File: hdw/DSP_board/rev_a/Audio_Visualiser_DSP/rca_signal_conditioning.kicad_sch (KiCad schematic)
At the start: 17 parts, among them J4 Left, J5 Right

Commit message: Annotated schematic
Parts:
- renumbered C62 to C1301, C63 to C1302, D14 to D1301, D15 to D1302, D16 to D1303, D17 to D1304, J4 to J1301, J5 to J1302, NT1 to NT1301, R61 to R1301, R62 to R1302, R63 to R1303, R64 to R1304, R65 to R1305, R66 to R1306, V1 to V1301, V6 to V1302
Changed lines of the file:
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@@
 		(dnp no)
 		(fields_autoplaced yes)
-		(property "Reference" "#PWR0221"
+		(property "Reference" "#PWR01306"
 			(at 149.86 55.88 0)
 			(hide yes)
@@
 			(project "Audio_Visualiser_DSP"
 				(path "/97a4dfb8-0e16-46f1-9709-8d2007dd0cd3/363750b9-a522-47db-9c7c-ad0a11bbbf3f"
-					(reference "#PWR0221")
+					(reference "#PWR01306")
 					(unit 1)
 				)
@@
 		(in_pos_files yes)
 		(dnp no)
-		(property "Reference" "#PWR0217"
+		(property "Reference" "#PWR01301"
 			(at 86.36 88.9 0)
 			(hide yes)
@@
 			(project "Audio_Visualiser_DSP"
 				(path "/97a4dfb8-0e16-46f1-9709-8d2007dd0cd3/363750b9-a522-47db-9c7c-ad0a11bbbf3f"
-					(reference "#PWR0217")
+					(reference "#PWR01301")
 					(unit 1)
 				)
@@
 		(in_pos_files yes)
 		(dnp no)
-		(property "Reference" "#PWR0314"
+		(property "Reference" "#PWR01302"
 			(at 86.36 152.4 0)
 			(hide yes)
@@
 			(project "Audio_Visualiser_DSP"
 				(path "/97a4dfb8-0e16-46f1-9709-8d2007dd0cd3/363750b9-a522-47db-9c7c-ad0a11bbbf3f"
-					(reference "#PWR0314")
+					(reference "#PWR01302")
 					(unit 1)
 				)
@@
 		(in_pos_files yes)
 		(dnp no)
-		(property "Reference" "V6"
+		(property "Reference" "V1302"
 			(at 88.9 138.43 0)
 			(show_name no)
@@
 			(project "Audio_Visualiser_DSP"
 				(path "/97a4dfb8-0e16-46f1-9709-8d2007dd0cd3/363750b9-a522-47db-9c7c-ad0a11bbbf3f"
-					(reference "V6")
+					(reference "V1302")
 					(unit 1)
 				)
@@
 		(dnp no)
 		(fields_autoplaced yes)
-		(property "Reference" "#PWR0220"
+		(property "Reference" "#PWR01305"
 			(at 133.35 152.4 0)
 			(hide yes)
@@
 			(project "Audio_Visualiser_DSP"
 				(path "/97a4dfb8-0e16-46f1-9709-8d2007dd0cd3/363750b9-a522-47db-9c7c-ad0a11bbbf3f"
-					(reference "#PWR0220")
+					(reference "#PWR01305")
 					(unit 1)
 				)
@@
 		(dnp no)
 		(fields_autoplaced yes)
-		(property "Reference" "C62"
+		(property "Reference" "C1301"
 			(at 124.46 46.99 90)
 			(show_name no)
@@
 			(project "Audio_Visualiser_DSP"
 				(path "/97a4dfb8-0e16-46f1-9709-8d2007dd0cd3/363750b9-a522-47db-9c7c-ad0a11bbbf3f"
-					(reference "C62")
+					(reference "C1301")
 					(unit 1)
 				)
@@
 		(dnp no)
 		(fields_autoplaced yes)
-		(property "Reference" "C63"
+		(property "Reference" "C1302"
 			(at 124.46 110.49 90)
 			(show_name no)
@@
 			(project "Audio_Visualiser_DSP"
 				(path "/97a4dfb8-0e16-46f1-9709-8d2007dd0cd3/363750b9-a522-47db-9c7c-ad0a11bbbf3f"
-					(reference "C63")
+					(reference "C1302")
 					(unit 1)
 				)
@@
 		(in_pos_files yes)
 		(dnp no)
-		(property "Reference" "#PWR0218"
+		(property "Reference" "#PWR01303"
 			(at 115.57 78.74 0)
 			(hide yes)
@@
 			(project "Audio_Visualiser_DSP"
 				(path "/97a4dfb8-0e16-46f1-9709-8d2007dd0cd3/363750b9-a522-47db-9c7c-ad0a11bbbf3f"
-					(reference "#PWR0218")
+					(reference "#PWR01303")
 					(unit 1)
 				)
@@
 		(dnp no)
 		(fields_autoplaced yes)
-		(property "Reference" "#PWR0222"
+		(property "Reference" "#PWR01307"
 			(at 149.86 119.38 0)
 			(hide yes)
@@
 			(project "Audio_Visualiser_DSP"
 				(path "/97a4dfb8-0e16-46f1-9709-8d2007dd0cd3/363750b9-a522-47db-9c7c-ad0a11bbbf3f"
-					(reference "#PWR0222")
+					(reference "#PWR01307")
 					(unit 1)
 				)
@@
 		(dnp no)
 		(fields_autoplaced yes)
-		(property "Reference" "J4"
+		(property "Reference" "J1301"
 			(at 73.9774 55.88 0)
 			(show_name no)
@@
 			(project "Audio_Visualiser_DSP"
 				(path "/97a4dfb8-0e16-46f1-9709-8d2007dd0cd3/363750b9-a522-47db-9c7c-ad0a11bbbf3f"
-					(reference "J4")
+					(reference "J1301")
 					(unit 1)
 				)
@@
 		(in_pos_files yes)
 		(dnp no)
-		(property "Reference" "R64"
+		(property "Reference" "R1304"
 			(at 135.89 123.19 90)
 			(show_name no)
@@
 			(project "Audio_Visualiser_DSP"
 				(path "/97a4dfb8-0e16-46f1-9709-8d2007dd0cd3/363750b9-a522-47db-9c7c-ad0a11bbbf3f"
-					(reference "R64")
+					(reference "R1304")
 					(unit 1)
 				)
@@
 		(in_pos_files yes)
 		(dnp no)
-		(property "Reference" "#PWR0219"
+		(property "Reference" "#PWR01304"
 			(at 115.57 142.24 0)
 			(hide yes)
@@
 			(project "Audio_Visualiser_DSP"
 				(path "/97a4dfb8-0e16-46f1-9709-8d2007dd0cd3/363750b9-a522-47db-9c7c-ad0a11bbbf3f"
-					(reference "#PWR0219")
+					(reference "#PWR01304")
 					(unit 1)
 				)
@@
 		(in_pos_files yes)
 		(dnp no)
-		(property "Reference" "#PWR0226"
+		(property "Reference" "#PWR01311"
 			(at 177.8 139.7 0)
 			(hide yes)
@@
 			(project "Audio_Visualiser_DSP"
 				(path "/97a4dfb8-0e16-46f1-9709-8d2007dd0cd3/363750b9-a522-47db-9c7c-ad0a11bbbf3f"
-					(reference "#PWR0226")
+					(reference "#PWR01311")
 					(unit 1)
 				)
@@
 		(in_pos_files yes)
 		(dnp no)
-		(property "Reference" "R62"
+		(property "Reference" "R1302"
 			(at 99.06 123.19 90)
 			(show_name no)
@@
 			(project "Audio_Visualiser_DSP"
 				(path "/97a4dfb8-0e16-46f1-9709-8d2007dd0cd3/363750b9-a522-47db-9c7c-ad0a11bbbf3f"
-					(reference "R62")
+					(reference "R1302")
 					(unit 1)
 				)
@@
 		(dnp no)
 		(fields_autoplaced yes)
-		(property "Reference" "D14"
+		(property "Reference" "D1301"
 			(at 118.11 67.3099 90)
 			(show_name no)
@@
 			(project "Audio_Visualiser_DSP"
 				(path "/97a4dfb8-0e16-46f1-9709-8d2007dd0cd3/363750b9-a522-47db-9c7c-ad0a11bbbf3f"
-					(reference "D14")
+					(reference "D1301")
 					(unit 1)
 				)
@@
 		(dnp no)
 		(fields_autoplaced yes)
-		(property "Reference" "D15"
+		(property "Reference" "D1302"
 			(at 118.11 130.8099 90)
 			(show_name no)
@@
 			(project "Audio_Visualiser_DSP"
 				(path "/97a4dfb8-0e16-46f1-9709-8d2007dd0cd3/363750b9-a522-47db-9c7c-ad0a11bbbf3f"
-					(reference "D15")
+					(reference "D1302")
 					(unit 1)
 				)
@@
 		(in_pos_files yes)
 		(dnp no)
-		(property "Reference" "V1"
+		(property "Reference" "V1301"
 			(at 88.9 74.93 0)
 			(show_name no)
@@
 			(project "Audio_Visualiser_DSP"
 				(path "/97a4dfb8-0e16-46f1-9709-8d2007dd0cd3/363750b9-a522-47db-9c7c-ad0a11bbbf3f"
-					(reference "V1")
+					(reference "V1301")
 					(unit 1)
 				)
@@
 		(in_pos_files yes)
 		(dnp no)
-		(property "Reference" "D17"
+		(property "Reference" "D1304"
 			(at 180.34 121.92 90)
 			(show_name no)
@@
 			(project "Audio_Visualiser_DSP"
 				(path "/97a4dfb8-0e16-46f1-9709-8d2007dd0cd3/363750b9-a522-47db-9c7c-ad0a11bbbf3f"
-					(reference "D17")
+					(reference "D1304")
 					(unit 1)
 				)
@@
 		(in_pos_files yes)
 		(dnp no)
-		(property "Reference" "#PWR0225"
+		(property "Reference" "#PWR01310"
 			(at 177.8 121.92 0)
 			(hide yes)
@@
 			(project "Audio_Visualiser_DSP"
 				(path "/97a4dfb8-0e16-46f1-9709-8d2007dd0cd3/363750b9-a522-47db-9c7c-ad0a11bbbf3f"
-					(reference "#PWR0225")
+					(reference "#PWR01310")
 					(unit 1)
 				)
@@
 		(in_pos_files yes)
 		(dnp no)
-		(property "Reference" "R63"
+		(property "Reference" "R1303"
 			(at 135.89 59.69 90)
 			(show_name no)
@@
 			(project "Audio_Visualiser_DSP"
 				(path "/97a4dfb8-0e16-46f1-9709-8d2007dd0cd3/363750b9-a522-47db-9c7c-ad0a11bbbf3f"
-					(reference "R63")
+					(reference "R1303")
 					(unit 1)
 				)
@@
 		(in_pos_files yes)
 		(dnp no)
-		(property "Reference" "R66"
+		(property "Reference" "R1306"
 			(at 151.638 116.078 0)
 			(show_name no)
@@
 			(project "Audio_Visualiser_DSP"
 				(path "/97a4dfb8-0e16-46f1-9709-8d2007dd0cd3/363750b9-a522-47db-9c7c-ad0a11bbbf3f"
-					(reference "R66")
+					(reference "R1306")
 					(unit 1)
 				)
@@
 		(in_pos_files yes)
 		(dnp no)
-		(property "Reference" "#PWR0223"
+		(property "Reference" "#PWR01308"
 			(at 177.8 58.42 0)
 			(hide yes)
@@
 			(project "Audio_Visualiser_DSP"
 				(path "/97a4dfb8-0e16-46f1-9709-8d2007dd0cd3/363750b9-a522-47db-9c7c-ad0a11bbbf3f"
-					(reference "#PWR0223")
+					(reference "#PWR01308")
 					(unit 1)
 				)
@@
 		(dnp no)
 		(fields_autoplaced yes)
-		(property "Reference" "NT1"
+		(property "Reference" "NT1301"
 			(at 124.46 147.32 0)
 			(show_name no)
@@
 			(project "Audio_Visualiser_DSP"
 				(path "/97a4dfb8-0e16-46f1-9709-8d2007dd0cd3/363750b9-a522-47db-9c7c-ad0a11bbbf3f"
-					(reference "NT1")
+					(reference "NT1301")
 					(unit 1)
 				)
@@
 		(in_pos_files yes)
 		(dnp no)
-		(property "Reference" "#PWR0224"
+		(property "Reference" "#PWR01309"
 			(at 177.8 76.2 0)
 			(hide yes)
@@
 			(project "Audio_Visualiser_DSP"
 				(path "/97a4dfb8-0e16-46f1-9709-8d2007dd0cd3/363750b9-a522-47db-9c7c-ad0a11bbbf3f"
-					(reference "#PWR0224")
+					(reference "#PWR01309")
 					(unit 1)
 				)
@@
 		(in_pos_files yes)
 		(dnp no)
-		(property "Reference" "D16"
+		(property "Reference" "D1303"
 			(at 180.34 58.42 90)
 			(show_name no)
@@
 			(project "Audio_Visualiser_DSP"
 				(path "/97a4dfb8-0e16-46f1-9709-8d2007dd0cd3/363750b9-a522-47db-9c7c-ad0a11bbbf3f"
-					(reference "D16")
+					(reference "D1303")
 					(unit 1)
 				)
@@
 		(in_pos_files yes)
 		(dnp no)
-		(property "Reference" "R61"
+		(property "Reference" "R1301"
 			(at 99.06 59.69 90)
 			(show_name no)
@@
 			(project "Audio_Visualiser_DSP"
 				(path "/97a4dfb8-0e16-46f1-9709-8d2007dd0cd3/363750b9-a522-47db-9c7c-ad0a11bbbf3f"
-					(reference "R61")
+					(reference "R1301")
 					(unit 1)
 				)
@@
 		(dnp no)
 		(fields_autoplaced yes)
-		(property "Reference" "J5"
+		(property "Reference" "J1302"
 			(at 73.9774 119.38 0)
 			(show_name no)
@@
 			(project "Audio_Visualiser_DSP"
 				(path "/97a4dfb8-0e16-46f1-9709-8d2007dd0cd3/363750b9-a522-47db-9c7c-ad0a11bbbf3f"
-					(reference "J5")
+					(reference "J1302")
 					(unit 2)
 				)
@@
 		(in_pos_files yes)
 		(dnp no)
-		(property "Reference" "R65"
+		(property "Reference" "R1305"
 			(at 151.638 52.578 0)
 			(show_name no)
@@
 			(project "Audio_Visualiser_DSP"
 				(path "/97a4dfb8-0e16-46f1-9709-8d2007dd0cd3/363750b9-a522-47db-9c7c-ad0a11bbbf3f"
-					(reference "R65")
+					(reference "R1305")
 					(unit 1)
 				)

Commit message: cleared stale digikey part numbers
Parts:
- C1301, C1302: footprint (none) -> Capacitors_SMD:C_0402; Digi-Key PN PN -> (none)
- R1301, R1302, R1303, R1304: footprint (none) -> Resistors_SMD:R_0402; Digi-Key PN PN -> (none)
- R1305, R1306: Digi-Key PN 541-100KHCT-ND -> (none)
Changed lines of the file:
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@@
 			)
 		)
-		(property "Footprint" ""
+		(property "Footprint" "Capacitors_SMD:C_0402"
 			(at 128.27 61.2648 0)
 			(hide yes)
@@
 			)
 		)
-		(property "Digi-Key PN" "PN"
+		(property "Digi-Key PN" ""
 			(at 111.76 51.435 0)
 			(hide yes)
@@
 			)
 		)
-		(property "Footprint" ""
+		(property "Footprint" "Capacitors_SMD:C_0402"
 			(at 128.27 124.7648 0)
 			(hide yes)
@@
 			)
 		)
-		(property "Digi-Key PN" "PN"
+		(property "Digi-Key PN" ""
 			(at 111.76 114.935 0)
 			(hide yes)
@@
 			)
 		)
-		(property "Footprint" ""
+		(property "Footprint" "Resistors_SMD:R_0402"
 			(at 135.89 125.73 0)
 			(hide yes)
@@
 			)
 		)
-		(property "Digi-Key PN" "PN"
+		(property "Digi-Key PN" ""
 			(at 146.05 133.35 0)
 			(hide yes)
@@
 			)
 		)
-		(property "Footprint" ""
+		(property "Footprint" "Resistors_SMD:R_0402"
 			(at 99.06 125.73 0)
 			(hide yes)
@@
 			)
 		)
-		(property "Digi-Key PN" "PN"
+		(property "Digi-Key PN" ""
 			(at 109.22 133.35 0)
 			(hide yes)
@@
 			)
 		)
-		(property "Footprint" ""
+		(property "Footprint" "Resistors_SMD:R_0402"
 			(at 135.89 62.23 0)
 			(hide yes)
@@
 			)
 		)
-		(property "Digi-Key PN" "PN"
+		(property "Digi-Key PN" ""
 			(at 146.05 69.85 0)
 			(hide yes)
@@
 			)
 		)
-		(property "Digi-Key PN" "541-100KHCT-ND"
+		(property "Digi-Key PN" ""
 			(at 149.86 119.38 0)
 			(hide yes)
@@
 			)
 		)
-		(property "Footprint" ""
+		(property "Footprint" "Resistors_SMD:R_0402"
 			(at 99.06 62.23 0)
 			(hide yes)
@@
 			)
 		)
-		(property "Digi-Key PN" "PN"
+		(property "Digi-Key PN" ""
 			(at 109.22 69.85 0)
 			(hide yes)
@@
 			)
 		)
-		(property "Digi-Key PN" "541-100KHCT-ND"
+		(property "Digi-Key PN" ""
 			(at 149.86 55.88 0)
 			(hide yes)

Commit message: updated rca jack
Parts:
- removed J1301: Left, symbol Connector:Conn_Coaxial_x2_Isolated
- removed J1302: Right, symbol Connector:Conn_Coaxial_x2_Isolated
- removed V1301, V1302: VSIN, symbol Simulation_SPICE:VSIN
- added J1301: Switchcraft_PJRAN2X1U_X, rca_jack:Switchcraft_PJRAN2X1U_X, symbol rca_jack:Switchcraft_PJRAN2X1U_X
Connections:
- net LEFT_RCA_SGND: now also J1301.4 (Sleeve_B)
- net RIGHT_RCA_SGND: now also J1301.1 (Sleeve_A)
- net at R1302.2: now also J1301.2 (Tip_A)
- net at R1301.2: now also J1301.5 (Tip_B)
- no-connect marks 0 -> 2

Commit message: assigned many digi-key part numbers
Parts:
- C1301, C1302: Dielectric X7R -> X7S; Digi-Key PN (none) -> 445-9116-1-ND
- D1301, D1302: Digi-Key PN (none) -> F6444CT-ND
- D1303, D1304: Digi-Key PN (none) -> BAT54SWT1GOSCT-ND
- J1301: Digi-Key PN PJRAN2X1U01AUX -> SC2534-ND
- R1301, R1302: Digi-Key PN (none) -> 311-220LRCT-ND
- R1303, R1304, R1305, R1306: Digi-Key PN (none) -> 311-20.0KLRCT-ND
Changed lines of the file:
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@@
 			)
 		)
-		(property "Digi-Key PN" "PJRAN2X1U01AUX"
+		(property "Digi-Key PN" "SC2534-ND"
 			(at 73.66 62.23 0)
 			(hide yes)
@@
 			)
 		)
-		(property "Dielectric" "X7R"
+		(property "Dielectric" "X7S"
 			(at 124.46 57.15 90)
 			(show_name no)
@@
 			)
 		)
-		(property "Digi-Key PN" ""
+		(property "Digi-Key PN" "445-9116-1-ND"
 			(at 111.76 51.435 0)
 			(hide yes)
@@
 			)
 		)
-		(property "Dielectric" "X7R"
+		(property "Dielectric" "X7S"
 			(at 124.46 120.65 90)
 			(show_name no)
@@
 			)
 		)
-		(property "Digi-Key PN" ""
+		(property "Digi-Key PN" "445-9116-1-ND"
 			(at 111.76 114.935 0)
 			(hide yes)
@@
 			)
 		)
-		(property "Digi-Key PN" ""
+		(property "Digi-Key PN" "311-20.0KLRCT-ND"
 			(at 146.05 133.35 0)
 			(hide yes)
@@
 			)
 		)
-		(property "Digi-Key PN" ""
+		(property "Digi-Key PN" "311-220LRCT-ND"
 			(at 109.22 133.35 0)
 			(hide yes)
@@
 			)
 		)
+		(property "Digi-Key PN" "F6444CT-ND"
+			(at 115.57 68.58 0)
+			(hide yes)
+			(show_name no)
+			(do_not_autoplace no)
+			(effects
+				(font
+					(size 1.27 1.27)
+				)
+			)
+		)
 		(pin "1"
 		)
@@
 			)
 		)
+		(property "Digi-Key PN" "F6444CT-ND"
+			(at 115.57 132.08 0)
+			(hide yes)
+			(show_name no)
+			(do_not_autoplace no)
+			(effects
+				(font
+					(size 1.27 1.27)
+				)
+			)
+		)
 		(pin "1"
 		)
@@
 			)
 		)
+		(property "Digi-Key PN" "BAT54SWT1GOSCT-ND"
+			(at 177.8 125.73 0)
+			(hide yes)
+			(show_name no)
+			(do_not_autoplace no)
+			(effects
+				(font
+					(size 1.27 1.27)
+				)
+			)
+		)
 		(pin "2"
 		)
@@
 			)
 		)
-		(property "Digi-Key PN" ""
+		(property "Digi-Key PN" "311-20.0KLRCT-ND"
 			(at 146.05 69.85 0)
 			(hide yes)
@@
 			)
 		)
-		(property "Digi-Key PN" ""
+		(property "Digi-Key PN" "311-20.0KLRCT-ND"
 			(at 149.86 119.38 0)
 			(hide yes)
@@
 			)
 		)
+		(property "Digi-Key PN" "BAT54SWT1GOSCT-ND"
+			(at 177.8 62.23 0)
+			(hide yes)
+			(show_name no)
+			(do_not_autoplace no)
+			(effects
+				(font
+					(size 1.27 1.27)
+				)
+			)
+		)
 		(pin "2"
 		)
@@
 			)
 		)
-		(property "Digi-Key PN" ""
+		(property "Digi-Key PN" "311-220LRCT-ND"
 			(at 109.22 69.85 0)
 			(hide yes)
@@
 			)
 		)
-		(property "Digi-Key PN" "PJRAN2X1U01AUX"
+		(property "Digi-Key PN" "SC2534-ND"
 			(at 73.66 125.73 0)
 			(hide yes)
@@
 			)
 		)
-		(property "Digi-Key PN" ""
+		(property "Digi-Key PN" "311-20.0KLRCT-ND"
 			(at 149.86 55.88 0)
 			(hide yes)

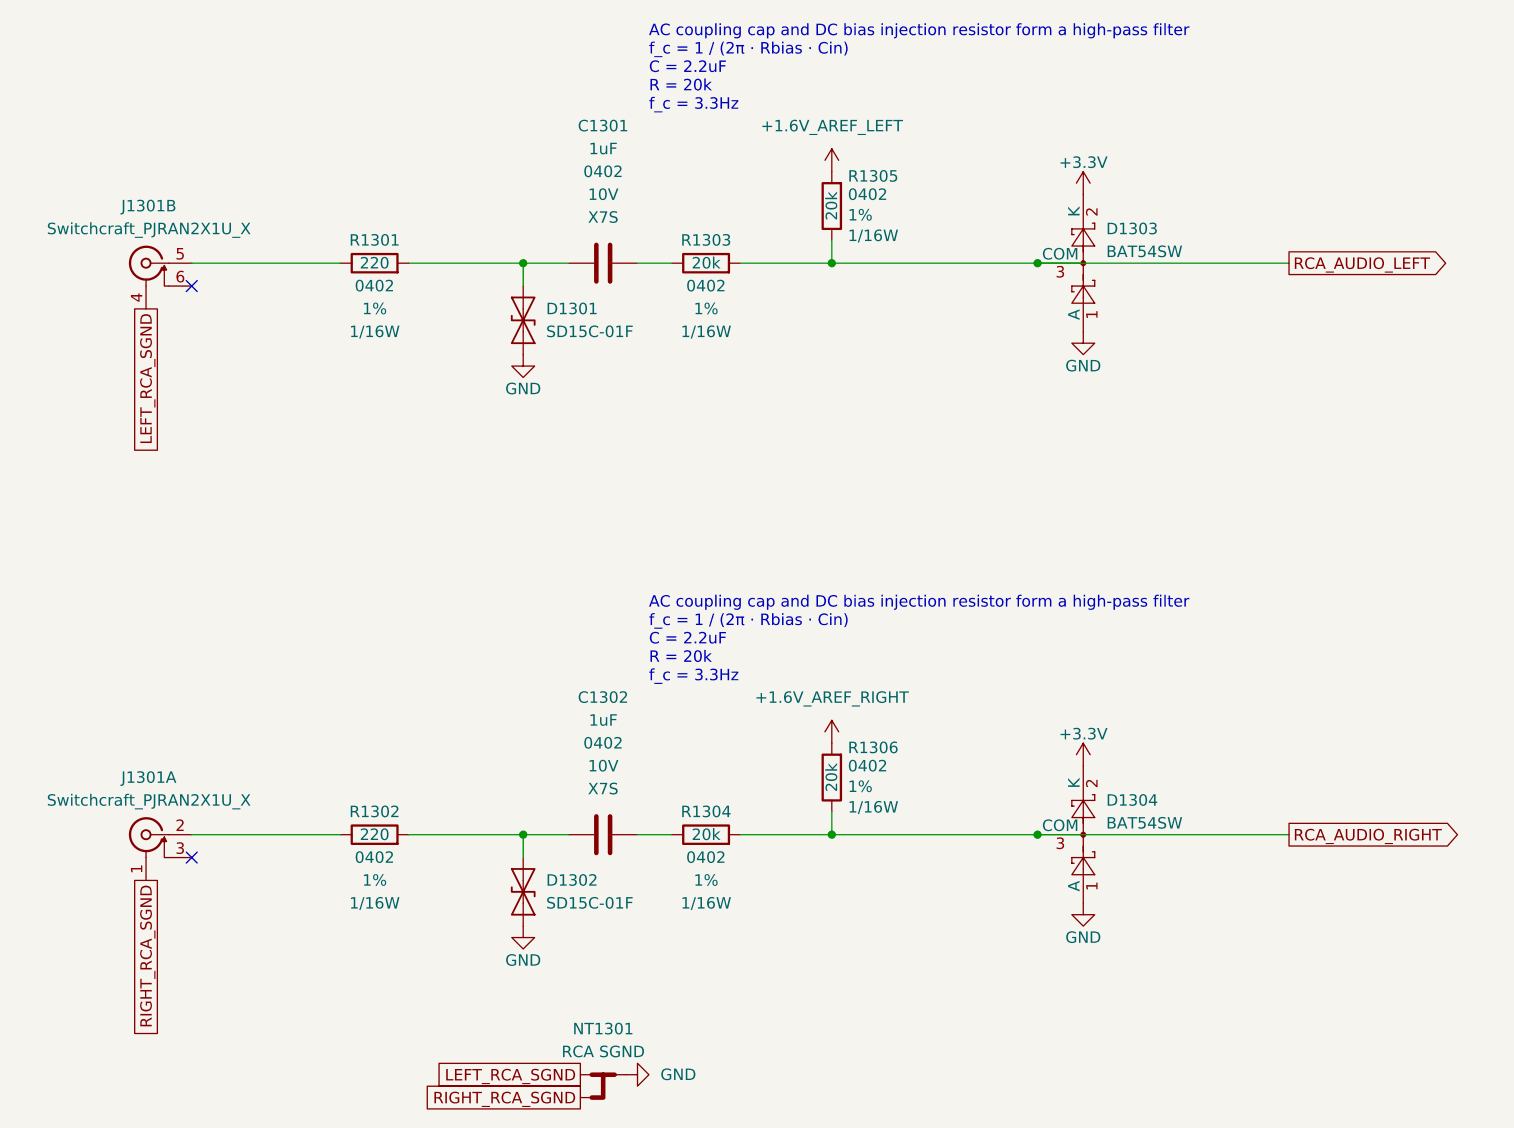
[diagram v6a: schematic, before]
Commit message: Added speaker signal path
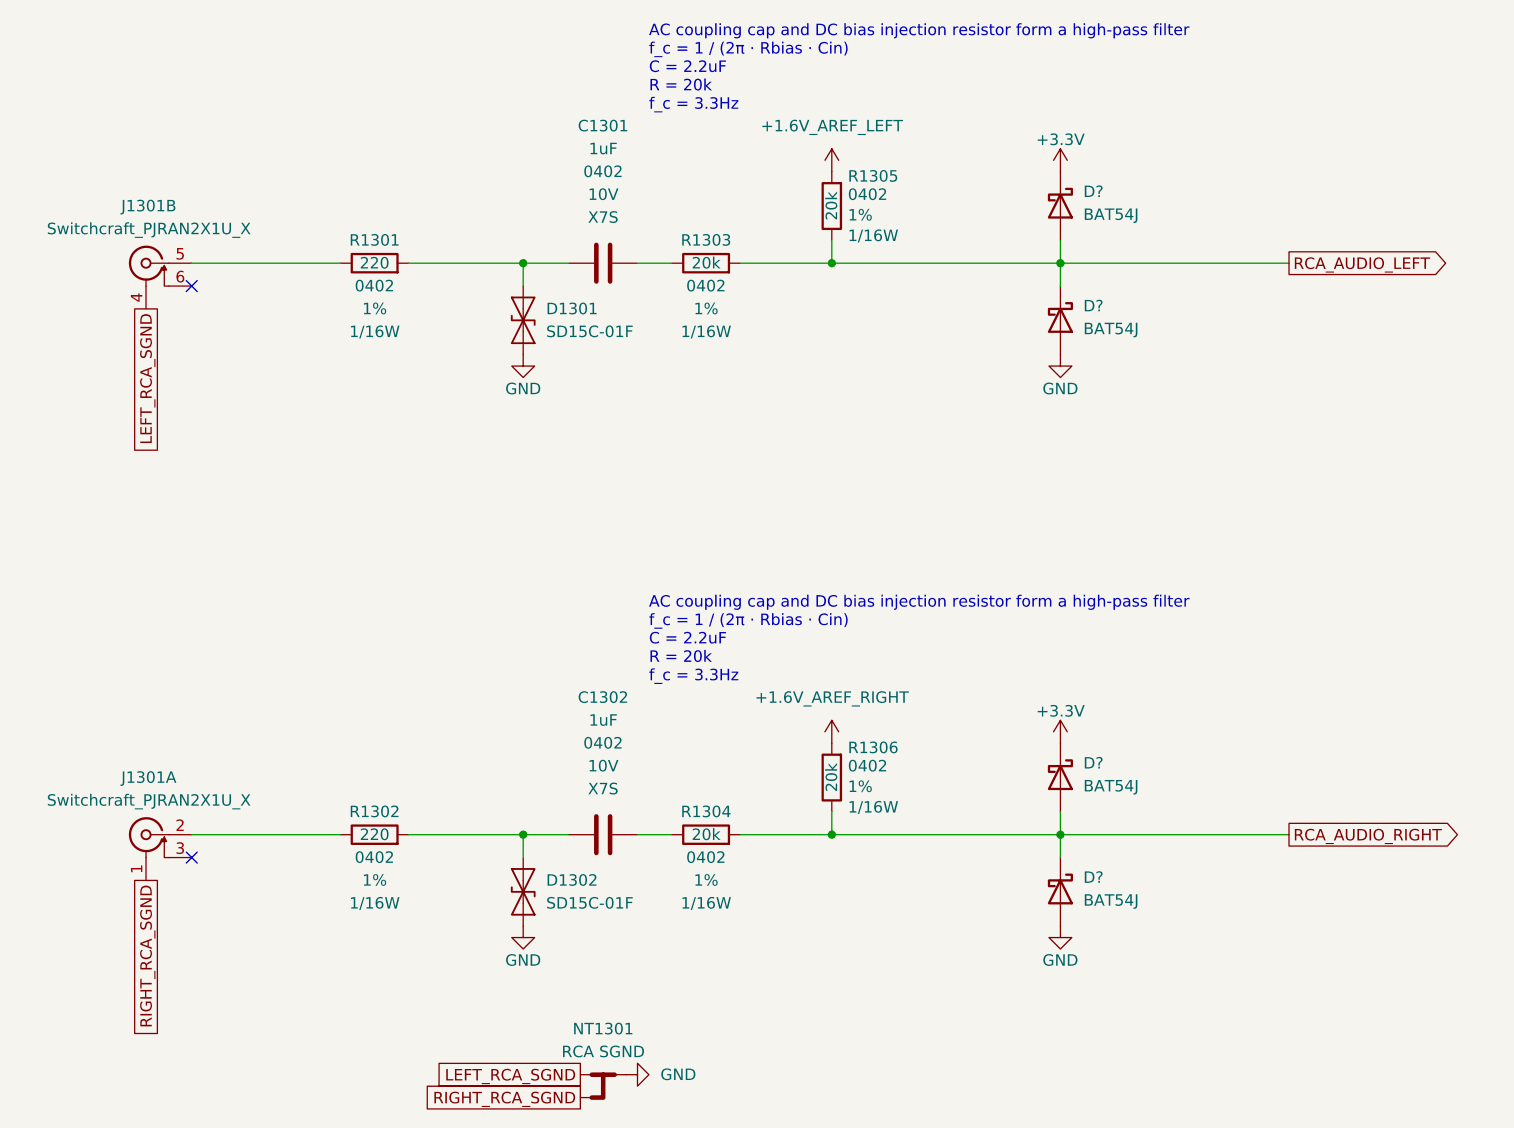
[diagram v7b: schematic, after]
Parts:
- removed D1303, D1304: BAT54SW, Package_TO_SOT_SMD:SOT-323_SC-70, symbol Diode:BAT54SW
- added D? (x4): BAT54J, Diode_SMD:D_SOD-323F, symbol Diode:BAT54J
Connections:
- net +3.3V: now also D?.1 (K), D?.1 (K)
- net GND: now also D?.2 (A), D?.2 (A)
- net RCA_AUDIO_LEFT: now also D?.1 (K), D?.2 (A)
- net RCA_AUDIO_RIGHT: now also D?.1 (K), D?.2 (A)
